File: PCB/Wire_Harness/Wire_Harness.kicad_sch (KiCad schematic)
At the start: 0 parts

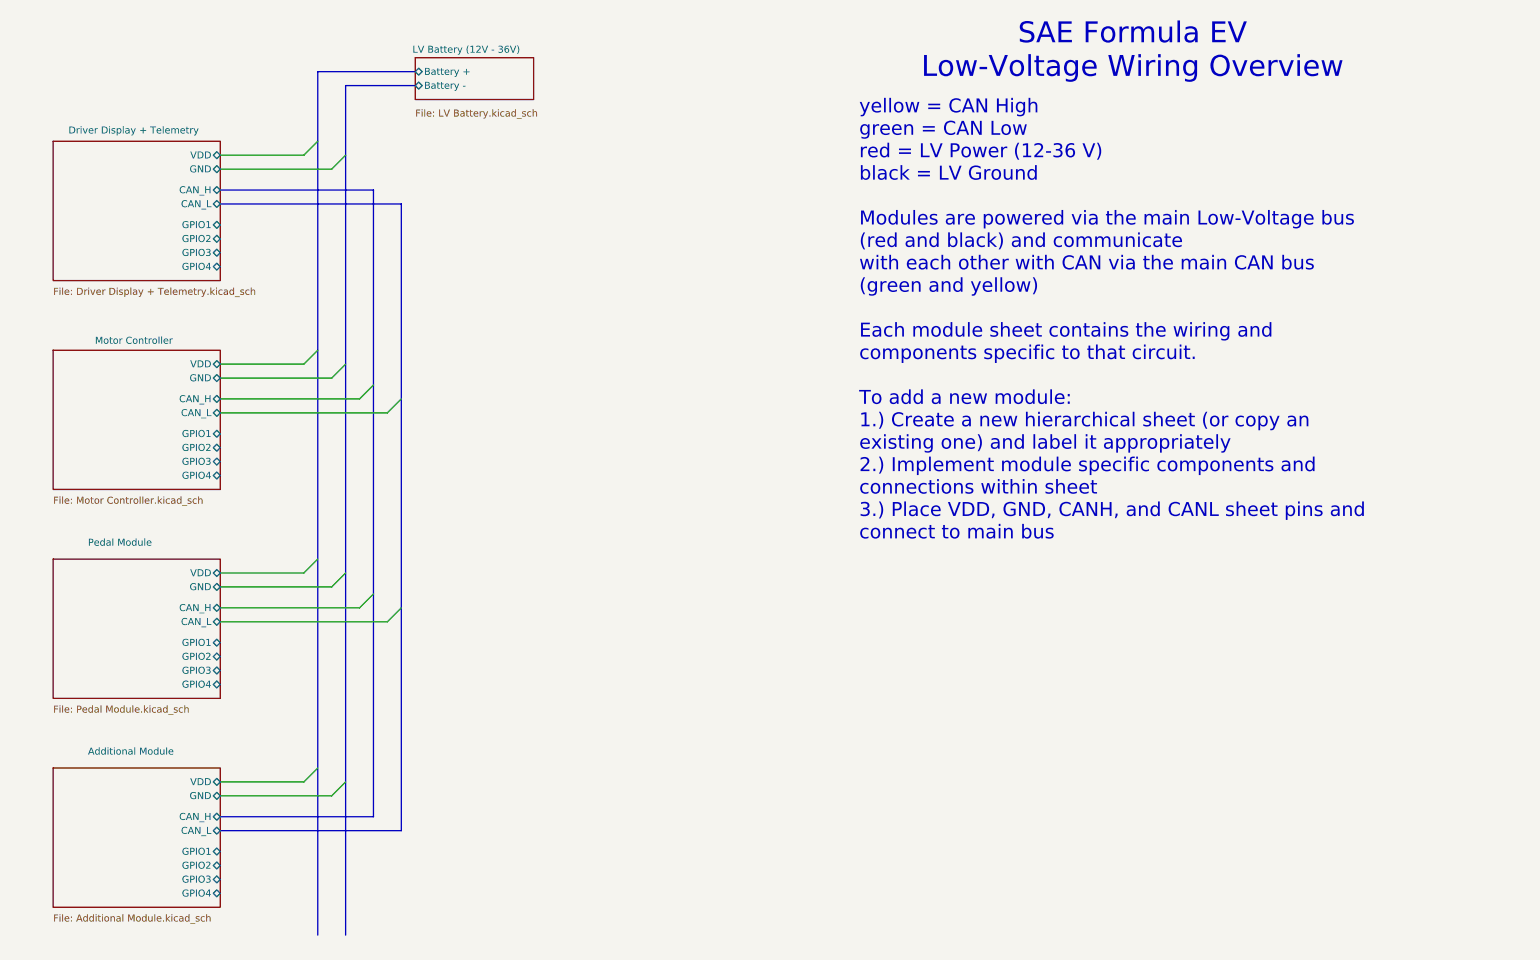
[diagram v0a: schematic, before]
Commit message: Adding molex connectors for main bus and modules
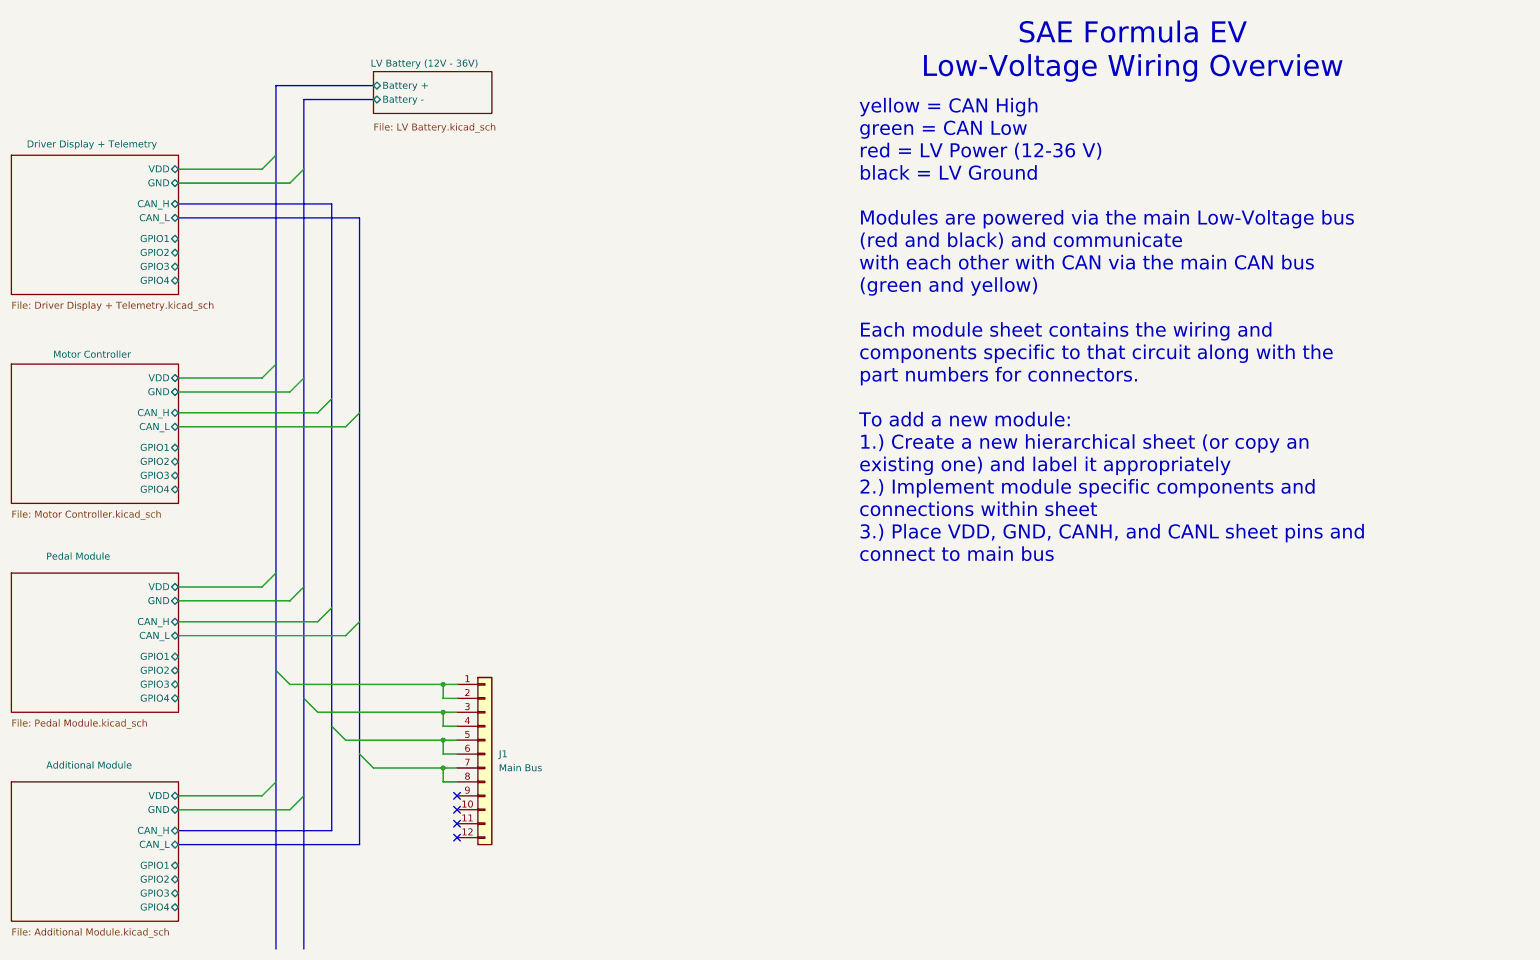
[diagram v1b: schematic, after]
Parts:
- added J1: Main Bus, symbol VMS_Symbols:Conn_01x12
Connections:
- new net: J1.1 (Pin_1), J1.2 (Pin_2)
- new net: J1.3 (Pin_3), J1.4 (Pin_4)
- new net: J1.5 (Pin_5), J1.6 (Pin_6)
- new net: J1.7 (Pin_7), J1.8 (Pin_8)
- no-connect marks 0 -> 4
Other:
- company: (none) -> Viking Motorsports
- title: (none) -> Formula EV Wiring Diagram

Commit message: Adding molex connectors for main bus and modules
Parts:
- J1: value Main Bus -> Main Bus Connector
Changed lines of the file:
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@@
 			)
 		)
-		(property "Value" "Main Bus"
+		(property "Value" "Main Bus Connector"
 			(at 109.22 152.3999 0)
 			(show_name no)

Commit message: changed schematic size to 11x17, added part numbers for enclosures and connectors
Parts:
- J1: value Main Bus Connector -> 334721206
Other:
- note added: "Enclosures and Connectors"
- moved on the sheet: J1
